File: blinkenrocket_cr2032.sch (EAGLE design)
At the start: 22 parts, among them SW1 SWITCH-4POMRON-6-6-SWITCH, SW2 SWITCH-4POMRON-6-6-SWITCH, U2 EEPROM-I2CEIAJ

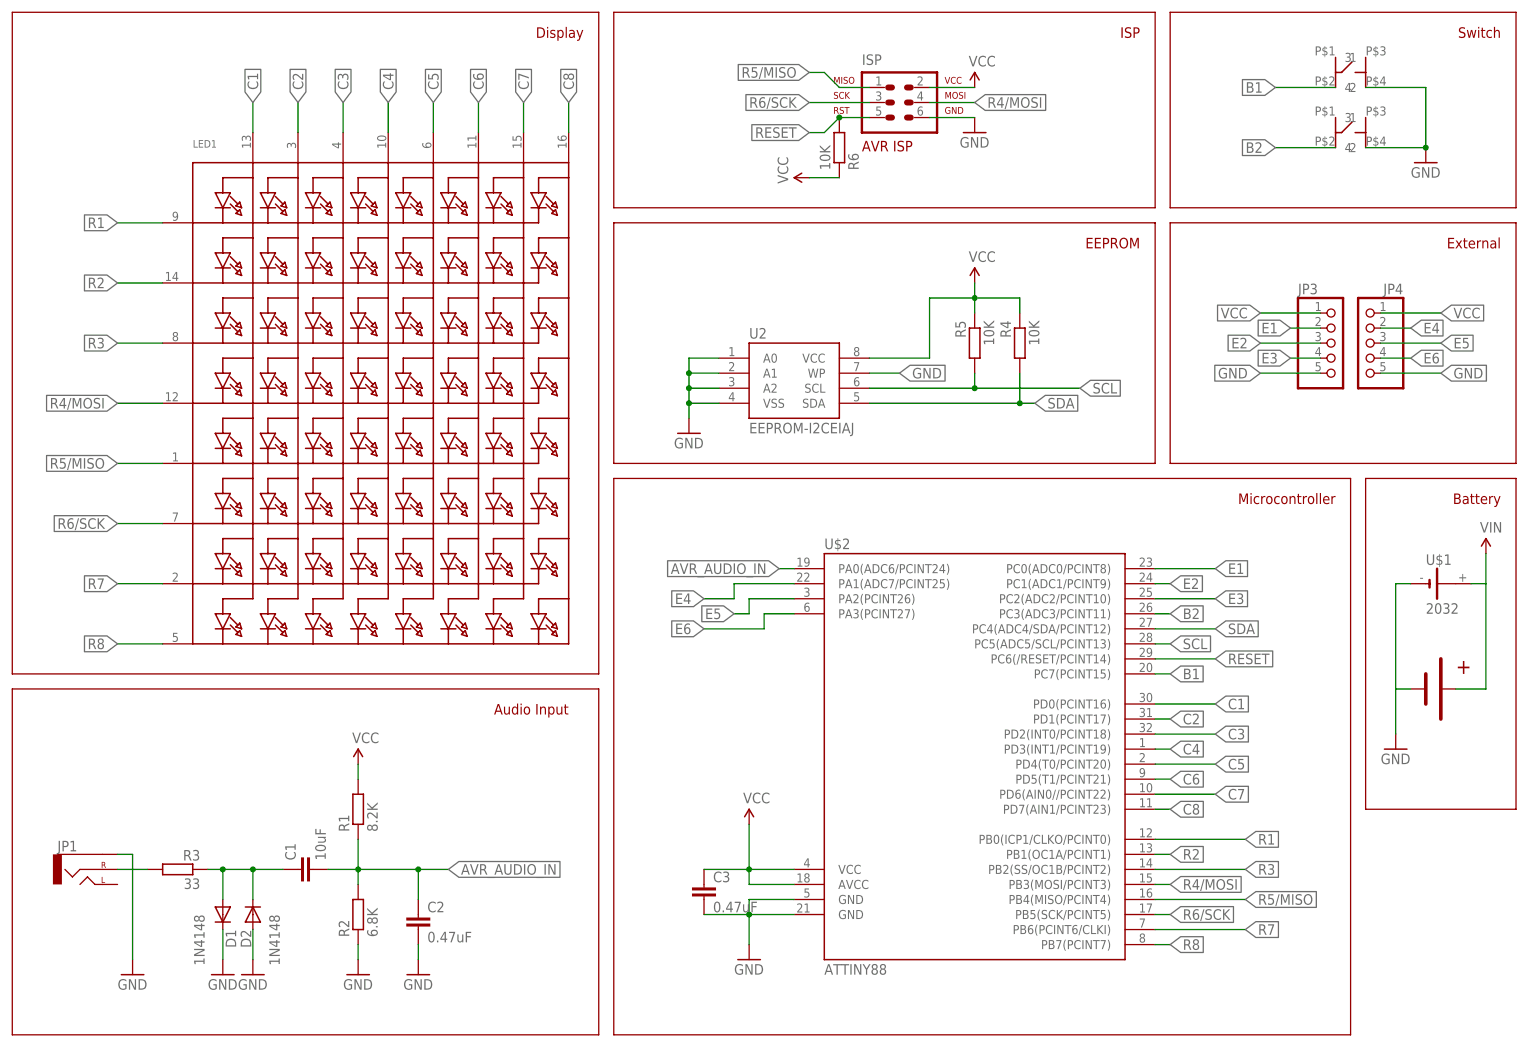
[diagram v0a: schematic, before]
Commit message: make the powersupply of the modem part switchable by the IC for powersaving reasons
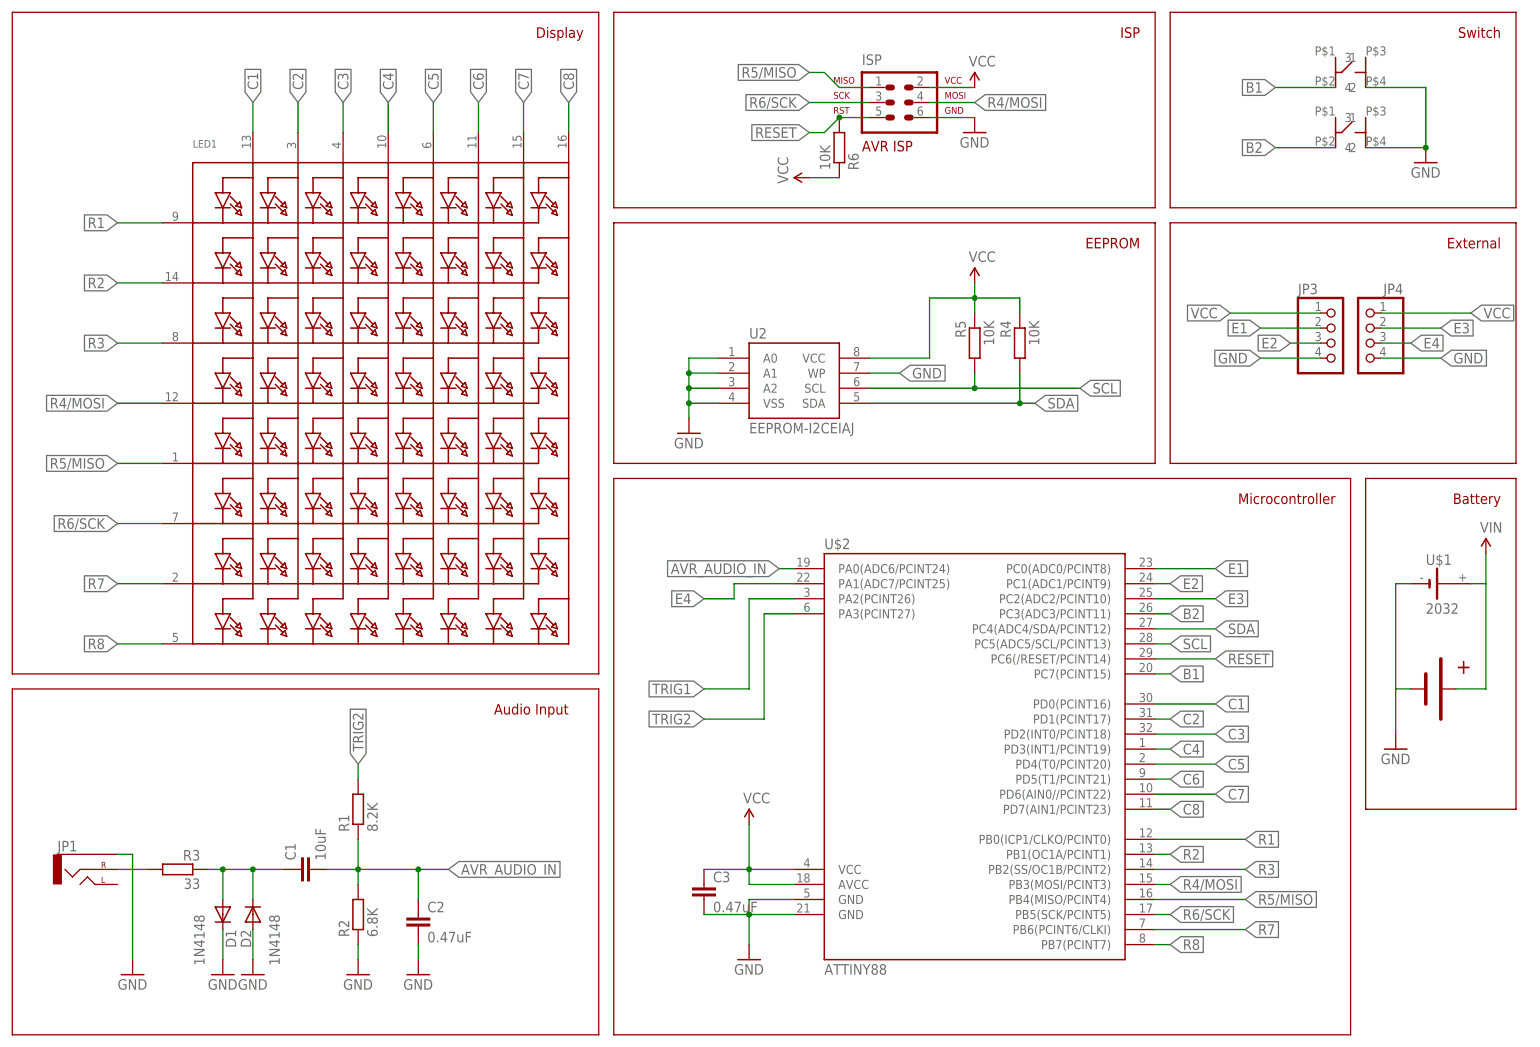
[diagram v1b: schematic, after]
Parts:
- JP3, JP4: device pinhead-2:PINHD-1X05_2.54-S -> pinhead-2:PINHD-1X04_2.54-S
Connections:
- removed net E5: JP4.3, U$2.PA2(PCINT26)
- removed net E6: JP4.4, U$2.PA3(PCINT27)
- new net TRIG1: U$2.PA2(PCINT26)
- new net TRIG2: R1.2, U$2.PA3(PCINT27)
- net E3: now also JP4.2; no longer JP3.4
- net E4: now also JP4.3; no longer JP4.2
- net GND: now also JP3.4, JP4.4; no longer JP3.5, JP4.5
- net VCC: no longer R1.2
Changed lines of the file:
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@@
 <part name="D1" library="diode-1" deviceset="DIODE-" device="SOD123" value="1N4148"/>
 <part name="GND3" library="SparkFun-Aesthetics" deviceset="GND" device=""/>
-<part name="SUPPLY1" library="SparkFun-Aesthetics" deviceset="VCC" device=""/>
 <part name="SUPPLY5" library="SparkFun-Aesthetics" deviceset="VCC" device=""/>
 <part name="GND4" library="SparkFun-Aesthetics" deviceset="GND" device=""/>
@@
 <part name="GND2" library="SparkFun-Aesthetics" deviceset="GND" device=""/>
 <part name="SUPPLY3" library="SparkFun-Aesthetics" deviceset="VCC" device=""/>
-<part name="JP3" library="pinhead-2" deviceset="PINHD-1X05" device="_2.54-S"/>
-<part name="JP4" library="pinhead-2" deviceset="PINHD-1X05" device="_2.54-S"/>
+<part name="JP3" library="pinhead-2" deviceset="PINHD-1X04" device="_2.54-S"/>
+<part name="JP4" library="pinhead-2" deviceset="PINHD-1X04" device="_2.54-S"/>
 <part name="R6" library="resistor" deviceset="R-EU_" device="R1206" value="10K"/>
 <part name="SUPPLY2" library="SparkFun-Aesthetics" deviceset="VCC" device=""/>
@@
 </instance>
 <instance part="GND3" gate="1" x="20.32" y="10.16"/>
-<instance part="SUPPLY1" gate="G$1" x="58.42" y="45.72"/>
 <instance part="SUPPLY5" gate="G$1" x="162.56" y="160.02"/>
 <instance part="GND4" gate="1" x="35.56" y="10.16"/>
@@
 <net name="VCC" class="0">
 <segment>
-<pinref part="R1" gate="G$1" pin="2"/>
-<pinref part="SUPPLY1" gate="G$1" pin="VCC"/>
-<wire x1="58.42" y1="45.72" x2="58.42" y2="43.18" width="0.1524" layer="91"/>
-</segment>
-<segment>
 <pinref part="SUPPLY5" gate="G$1" pin="VCC"/>
 <wire x1="162.56" y1="160.02" x2="154.94" y2="160.02" width="0.1524" layer="91"/>
@@
 </segment>
 <segment>
-<pinref part="JP3" gate="A" pin="1"/>
-<wire x1="220.98" y1="121.92" x2="210.82" y2="121.92" width="0.1524" layer="91"/>
-<label x="210.82" y="121.92" size="1.778" layer="95" rot="R180" xref="yes"/>
-</segment>
-<segment>
 <pinref part="JP4" gate="A" pin="1"/>
-<wire x1="231.14" y1="121.92" x2="241.3" y2="121.92" width="0.1524" layer="91"/>
-<label x="241.3" y="121.92" size="1.778" layer="95" xref="yes"/>
+<wire x1="231.14" y1="121.92" x2="246.38" y2="121.92" width="0.1524" layer="91"/>
+<label x="246.38" y="121.92" size="1.778" layer="95" xref="yes"/>
 </segment>
 <segment>
@@
 <pinref part="R6" gate="G$1" pin="1"/>
 <wire x1="134.62" y1="144.78" x2="139.7" y2="144.78" width="0.1524" layer="91"/>
+</segment>
+<segment>
+<pinref part="JP3" gate="A" pin="1"/>
+<wire x1="220.98" y1="121.92" x2="205.74" y2="121.92" width="0.1524" layer="91"/>
+<label x="205.74" y="121.92" size="1.778" layer="95" rot="R180" xref="yes"/>
 </segment>
 </net>
@@
 </segment>
 <segment>
-<pinref part="JP3" gate="A" pin="5"/>
-<wire x1="220.98" y1="111.76" x2="210.82" y2="111.76" width="0.1524" layer="91"/>
-<label x="210.82" y="111.76" size="1.778" layer="95" rot="R180" xref="yes"/>
-</segment>
-<segment>
-<pinref part="JP4" gate="A" pin="5"/>
-<wire x1="231.14" y1="111.76" x2="241.3" y2="111.76" width="0.1524" layer="91"/>
-<label x="241.3" y="111.76" size="1.778" layer="95" xref="yes"/>
-</segment>
-<segment>
 <pinref part="GND10" gate="1" pin="GND"/>
 <wire x1="238.76" y1="160.02" x2="238.76" y2="149.86" width="0.1524" layer="91"/>
@@
 <wire x1="228.6" y1="149.86" x2="238.76" y2="149.86" width="0.1524" layer="91"/>
 <junction x="238.76" y="149.86"/>
+</segment>
+<segment>
+<pinref part="JP3" gate="A" pin="4"/>
+<wire x1="220.98" y1="114.3" x2="210.82" y2="114.3" width="0.1524" layer="91"/>
+<label x="210.82" y="114.3" size="1.778" layer="95" rot="R180" xref="yes"/>
+</segment>
+<segment>
+<pinref part="JP4" gate="A" pin="4"/>
+<wire x1="231.14" y1="114.3" x2="241.3" y2="114.3" width="0.1524" layer="91"/>
+<label x="241.3" y="114.3" size="1.778" layer="95" xref="yes"/>
 </segment>
 </net>
@@
 </segment>
 <segment>
-<pinref part="JP3" gate="A" pin="4"/>
-<wire x1="220.98" y1="114.3" x2="215.9" y2="114.3" width="0.1524" layer="91"/>
-<label x="215.9" y="114.3" size="1.778" layer="95" rot="R180" xref="yes"/>
+<pinref part="JP4" gate="A" pin="2"/>
+<wire x1="231.14" y1="119.38" x2="241.3" y2="119.38" width="0.1524" layer="91"/>
+<label x="241.3" y="119.38" size="1.778" layer="95" xref="yes"/>
 </segment>
 </net>
@@
 <segment>
 <pinref part="JP3" gate="A" pin="3"/>
-<wire x1="220.98" y1="116.84" x2="210.82" y2="116.84" width="0.1524" layer="91"/>
-<label x="210.82" y="116.84" size="1.778" layer="95" rot="R180" xref="yes"/>
+<wire x1="220.98" y1="116.84" x2="215.9" y2="116.84" width="0.1524" layer="91"/>
+<label x="215.9" y="116.84" size="1.778" layer="95" rot="R180" xref="yes"/>
 </segment>
 </net>
@@
 <segment>
 <pinref part="JP3" gate="A" pin="2"/>
-<wire x1="220.98" y1="119.38" x2="215.9" y2="119.38" width="0.1524" layer="91"/>
-<label x="215.9" y="119.38" size="1.778" layer="95" rot="R180" xref="yes"/>
+<wire x1="220.98" y1="119.38" x2="210.82" y2="119.38" width="0.1524" layer="91"/>
+<label x="210.82" y="119.38" size="1.778" layer="95" rot="R180" xref="yes"/>
 </segment>
 </net>
@@
 </segment>
 <segment>
-<pinref part="JP4" gate="A" pin="2"/>
-<wire x1="231.14" y1="119.38" x2="236.22" y2="119.38" width="0.1524" layer="91"/>
-<label x="236.22" y="119.38" size="1.778" layer="95" xref="yes"/>
-</segment>
-</net>
-<net name="E5" class="0">
+<pinref part="JP4" gate="A" pin="3"/>
+<wire x1="231.14" y1="116.84" x2="236.22" y2="116.84" width="0.1524" layer="91"/>
+<label x="236.22" y="116.84" size="1.778" layer="95" xref="yes"/>
+</segment>
+</net>
+<net name="TRIG1" class="0">
 <segment>
 <pinref part="U$2" gate="G$1" pin="PA2(PCINT26)"/>
 <wire x1="132.08" y1="73.66" x2="124.46" y2="73.66" width="0.1524" layer="91"/>
-<wire x1="124.46" y1="73.66" x2="124.46" y2="71.12" width="0.1524" layer="91"/>
-<wire x1="124.46" y1="71.12" x2="121.92" y2="71.12" width="0.1524" layer="91"/>
-<label x="121.92" y="71.12" size="1.778" layer="95" rot="R180" xref="yes"/>
-</segment>
-<segment>
-<pinref part="JP4" gate="A" pin="3"/>
-<wire x1="231.14" y1="116.84" x2="241.3" y2="116.84" width="0.1524" layer="91"/>
-<label x="241.3" y="116.84" size="1.778" layer="95" xref="yes"/>
-</segment>
-</net>
-<net name="E6" class="0">
+<wire x1="124.46" y1="73.66" x2="124.46" y2="58.42" width="0.1524" layer="91"/>
+<wire x1="124.46" y1="58.42" x2="116.84" y2="58.42" width="0.1524" layer="91"/>
+<label x="116.84" y="58.42" size="1.778" layer="95" rot="R180" xref="yes"/>
+</segment>
+</net>
+<net name="TRIG2" class="0">
 <segment>
 <pinref part="U$2" gate="G$1" pin="PA3(PCINT27)"/>
 <wire x1="132.08" y1="71.12" x2="127" y2="71.12" width="0.1524" layer="91"/>
-<wire x1="127" y1="71.12" x2="127" y2="68.58" width="0.1524" layer="91"/>
-<wire x1="127" y1="68.58" x2="116.84" y2="68.58" width="0.1524" layer="91"/>
-<label x="116.84" y="68.58" size="1.778" layer="95" rot="R180" xref="yes"/>
-</segment>
-<segment>
-<pinref part="JP4" gate="A" pin="4"/>
-<wire x1="231.14" y1="114.3" x2="236.22" y2="114.3" width="0.1524" layer="91"/>
-<label x="236.22" y="114.3" size="1.778" layer="95" xref="yes"/>
-</segment>
-</net>
+<wire x1="127" y1="71.12" x2="127" y2="53.34" width="0.1524" layer="91"/>
+<wire x1="127" y1="53.34" x2="116.84" y2="53.34" width="0.1524" layer="91"/>
+<label x="116.84" y="53.34" size="1.778" layer="95" rot="R180" xref="yes"/>
+</segment>
+<segment>
+<pinref part="R1" gate="G$1" pin="2"/>
+<wire x1="58.42" y1="43.18" x2="58.42" y2="45.72" width="0.1524" layer="91"/>
+<label x="58.42" y="45.72" size="1.778" layer="95" rot="R90" xref="yes"/>
+</segment>
+</net>

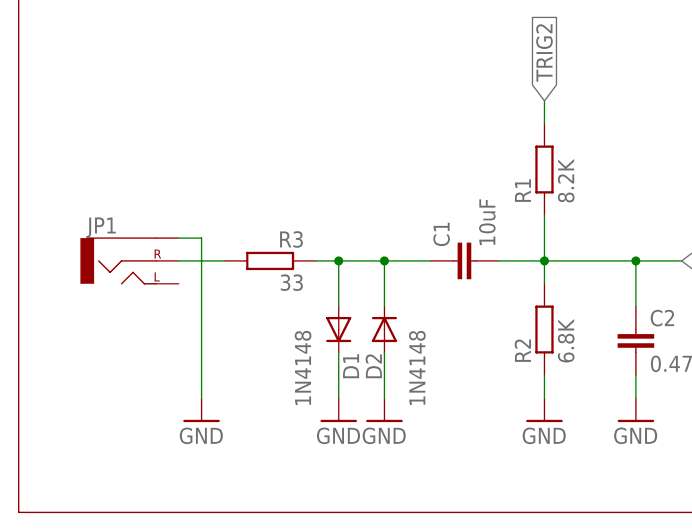
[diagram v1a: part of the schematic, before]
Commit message: change value of modem input resistor
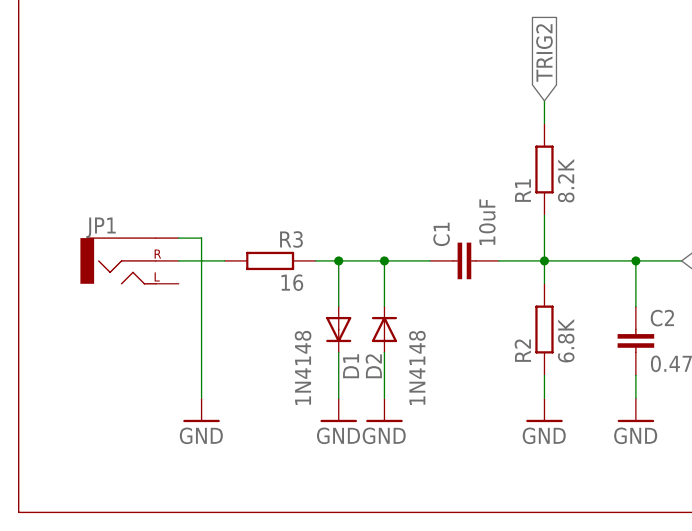
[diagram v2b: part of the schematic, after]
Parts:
- R3: value 33 -> 16
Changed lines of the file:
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@@
 <part name="R1" library="resistor" deviceset="R-EU_" device="R1206" value="8.2K"/>
 <part name="R2" library="resistor" deviceset="R-EU_" device="R1206" value="6.8K"/>
-<part name="R3" library="resistor" deviceset="R-EU_" device="R1206" value="33"/>
+<part name="R3" library="resistor" deviceset="R-EU_" device="R1206" value="16"/>
 <part name="D2" library="diode-1" deviceset="DIODE-" device="SOD123" value="1N4148"/>
 <part name="D1" library="diode-1" deviceset="DIODE-" device="SOD123" value="1N4148"/>

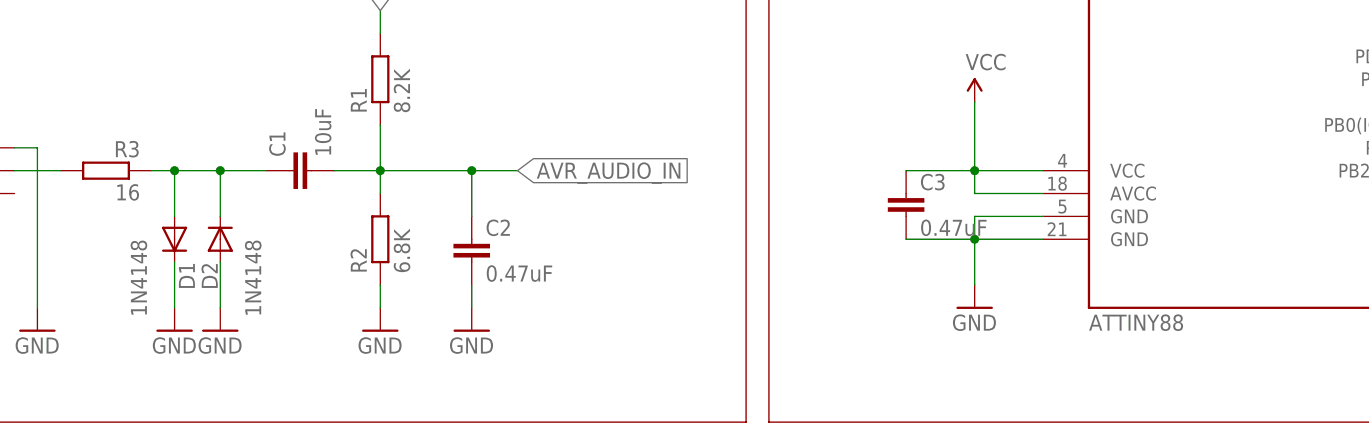
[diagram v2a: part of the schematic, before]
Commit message: Revision 2c - diodes do have positioning information now - added blinkenrocket.de text - add IC component name
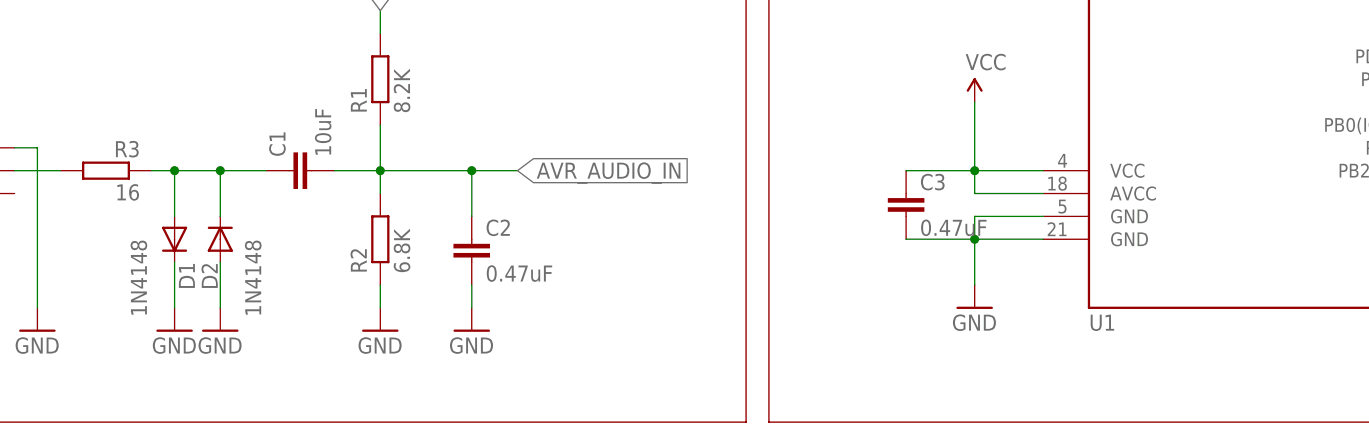
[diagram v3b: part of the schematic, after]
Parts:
- D1, D2: device diode-1:DIODE-SOD123 -> ipc-7351-diode:DIODE_SOD-123
- U$2: value ATTINY88 -> U1
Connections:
- net GND: now also D1.K; no longer D1.C
- net N$3: now also D2.K; no longer D2.C
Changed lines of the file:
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@@
 <part name="R2" library="resistor" deviceset="R-EU_" device="R1206" value="6.8K"/>
 <part name="R3" library="resistor" deviceset="R-EU_" device="R1206" value="16"/>
-<part name="D2" library="diode-1" deviceset="DIODE-" device="SOD123" value="1N4148"/>
-<part name="D1" library="diode-1" deviceset="DIODE-" device="SOD123" value="1N4148"/>
+<part name="D2" library="ipc-7351-diode" deviceset="DIODE_" device="SOD-123" value="1N4148"/>
+<part name="D1" library="ipc-7351-diode" deviceset="DIODE_" device="SOD-123" value="1N4148"/>
 <part name="GND3" library="SparkFun-Aesthetics" deviceset="GND" device=""/>
 <part name="SUPPLY5" library="SparkFun-Aesthetics" deviceset="VCC" device=""/>
@@
 <part name="SW1" library="switch" deviceset="SWITCH-4P" device="OMRON-6-6-SWITCH"/>
 <part name="ISP" library="avr-7" deviceset="AVR-ISP-6" device="VERT"/>
-<part name="U$2" library="avr-muzy" deviceset="TINY48/88" device="B" value="ATTINY88"/>
+<part name="U$2" library="avr-muzy" deviceset="TINY48/88" device="B" value="U1"/>
 <part name="U2" library="SparkFun-DigitalIC" deviceset="EEPROM-I2C" device="EIAJ"/>
 <part name="R4" library="resistor" deviceset="R-EU_" device="R1206" value="10K"/>
@@
 </segment>
 <segment>
-<pinref part="D1" gate="G$1" pin="C"/>
+<pinref part="D1" gate="G$1" pin="K"/>
 <pinref part="GND4" gate="1" pin="GND"/>
 <wire x1="35.56" y1="17.78" x2="35.56" y2="12.7" width="0.1524" layer="91"/>
@@
 <wire x1="33.02" y1="27.94" x2="35.56" y2="27.94" width="0.1524" layer="91"/>
 <wire x1="35.56" y1="27.94" x2="35.56" y2="22.86" width="0.1524" layer="91"/>
-<pinref part="D2" gate="G$1" pin="C"/>
+<pinref part="D2" gate="G$1" pin="K"/>
 <pinref part="C1" gate="G$1" pin="1"/>
 <wire x1="40.64" y1="22.86" x2="40.64" y2="27.94" width="0.1524" layer="91"/>
